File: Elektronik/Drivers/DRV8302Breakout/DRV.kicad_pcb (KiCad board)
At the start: 2 copper layers, 44.4 x 53.3 mm, 55 parts, among them J1 CONN_02X18, J2 CONN_02X12, J3 CONN_02X16, J4 CONN_01X04_MALE, J5 CONN_01X04_MALE, J6 Conn_01x02_Male, U2 TC2117, U3 DRV8302

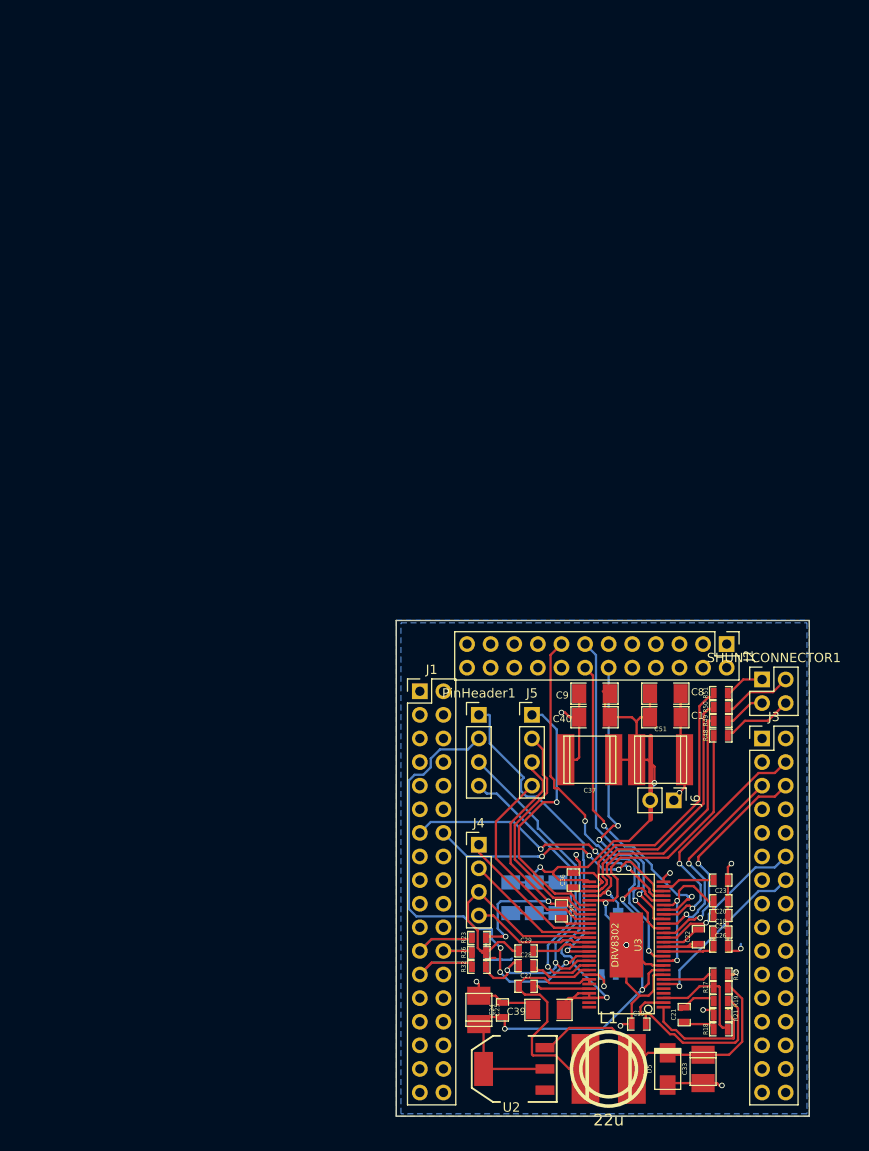
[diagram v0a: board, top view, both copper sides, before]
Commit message: first driver pcb most things routed missnig power connector
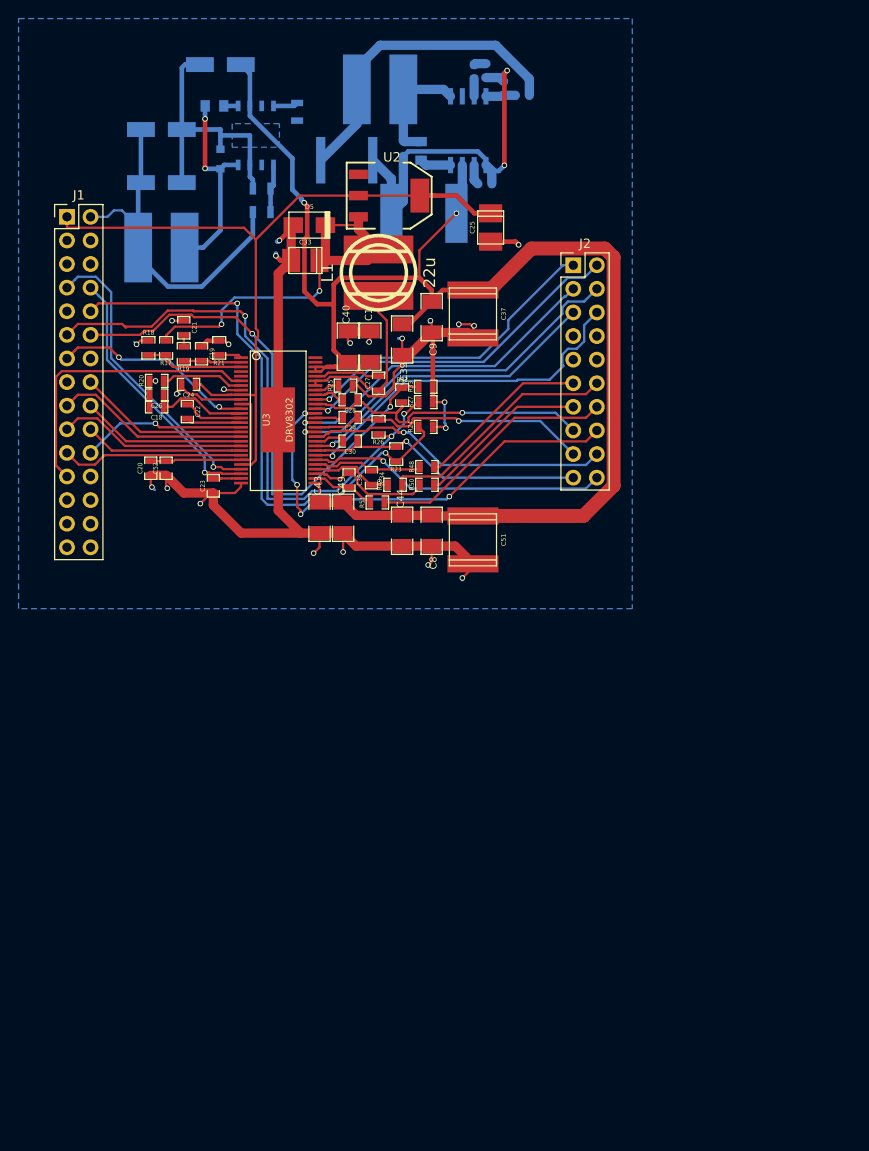
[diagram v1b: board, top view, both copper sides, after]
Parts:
- removed J3: CONN_02X16, Pin_Headers:Pin_Header_Straight_2x16_Pitch2.54mm
- removed J4, J5, PinHeader1: CONN_01X04_MALE, Pin_Headers:Pin_Header_Straight_1x04_Pitch2.54mm
- removed J6: Conn_01x02_Male, Pin_Headers:Pin_Header_Straight_1x02_Pitch2.54mm
- removed SHUNTCONNECTOR1: CONN_01X04_MALE, Pin_Headers:Pin_Header_Straight_2x02_Pitch2.54mm
- added C2: 22μ, Capacitors_SMD:C_2220, B.Cu at (167.4, 38.1)
- added C3: 470pF, Capacitors_SMD:C_0603, B.Cu at (181.1, 28.6)
- added C4: 100nF, Capacitors_SMD:C_0805, B.Cu at (175.4, 37.1)
- added C5: 10μF, Capacitors_SMD:C_2225_HandSoldering, B.Cu at (175.7, 43.8)
- added C6: 10μF, Capacitors_SMD:CP_Elec_5x5.3, B.Cu at (153.8, 27.8)
- added C7: 0.1μF, Capacitors_SMD:C_0805, B.Cu at (153.2, 32.3)
- added Cout1: 33μF, Capacitors_SMD:CP_Elec_5x5.3, B.Cu at (147.4, 34.8)
- added Cout2: 33μF, Capacitors_SMD:CP_Elec_5x5.3, B.Cu at (147.4, 40.5)
- added D1: D_Schottky, Diodes_SMD:D_0603, B.Cu at (173.5, 36.8)
- added D2: D_Schottky_75V, Diodes_SMD:D_0805, B.Cu at (153.8, 38.0)
- added L2: 10μ, w_smd_inductors:inductor_smd_8x5mm, B.Cu at (171.0, 30.5)
- added L3: 10μH, w_smd_inductors:inductor_smd_8x5mm, B.Cu at (147.4, 47.5)
- added R1: 127k, Resistors_SMD:R_0603, B.Cu at (186.3, 31.1)
- added R2: 16k, Resistors_SMD:R_0603, B.Cu at (182.4, 28.5)
- added R3: 40.2k, Resistors_SMD:R_0603, B.Cu at (184.3, 30.4)
- added R4: 200k, Resistors_SMD:R_0603, B.Cu at (182.3, 40.6)
- added RFBB1: 17.8k, Resistors_SMD:R_0805, B.Cu at (158.2, 41.1)
- added RFBT1: 100k, Resistors_SMD:R_0805, B.Cu at (158.2, 43.7)
- added RT1: 41,2k, Resistors_SMD:R_0805, B.Cu at (162.1, 32.9)
- added U1: LMR16020, SMD_Packages:SOIC-8-N, B.Cu at (157.6, 35.4)
- added Ureg1: MP4559, Housings_SOIC:SO-8_5.3x6.2mm_Pitch1.27mm, B.Cu at (180.5, 34.9)
- C34, C43, C44, C49, R24, R25, R27, R33: moved to F.Cu
- J1: value CONN_02X18 -> CONN_CPU; footprint Pin_Headers:Pin_Header_Straight_2x18_Pitch2.54mm -> Pin_Headers:Pin_Header_Straight_2x15_Pitch2.54mm
- J2: value CONN_02X12 -> Conn_POWER; footprint Pin_Headers:Pin_Header_Straight_2x12_Pitch2.54mm -> Pin_Headers:Pin_Header_Straight_2x10_Pitch2.54mm
- moved D5 98.7 mm to (163.4, 45.1), turned to 0 degrees
- moved C33 97.0 mm to (162.9, 48.9), turned to 0 degrees
- moved R18 95.8 mm to (146.1, 58.3), turned to 90 degrees
- moved U2 94.9 mm to (172.0, 41.9), turned to 270 degrees
- moved C21 91.4 mm to (149.9, 56.1), turned to 270 degrees
- moved R17 91.1 mm to (148.0, 58.3), turned to 270 degrees
- moved R19 90.5 mm to (149.9, 58.9), turned to 270 degrees
- moved R21 89.8 mm to (153.7, 58.3), turned to 270 degrees
- moved L1 89.2 mm to (170.8, 50.2), turned to 90 degrees
- moved R20 88.1 mm to (146.9, 61.8), turned to 180 degrees
- moved C19 86.1 mm to (151.8, 58.9), turned to 270 degrees
- moved C26 84.9 mm to (146.9, 63.4), turned to 180 degrees
- moved C25 84.2 mm to (182.9, 45.3), turned to 90 degrees
- moved C18 82.9 mm to (146.9, 64.6), turned to 180 degrees
- moved C22 78.9 mm to (150.2, 65.2), turned to 270 degrees
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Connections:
- J1 pad 1: Net-(J1-Pad1) -> VCC
- J1 pad 10: Net-(J1-Pad10) -> /DRV/SENS1
- J1 pad 11: Net-(J1-Pad11) -> /DRV/SENS2
- J1 pad 12: Net-(J1-Pad12) -> /DRV/SENS3
- J1 pad 13: /CJMCU_PINS/BR_S01 -> /DRV/DC_CAL
- J1 pad 14: /CJMCU_PINS/BR_S02 -> (no net)
- J1 pad 15: /CJMCU_PINS/LED_RED -> (no net)
- J1 pad 16: /CJMCU_PINS/LED_GREEN -> /DRV/H1
- J1 pad 17: Net-(J1-Pad17) -> /DRV/L1
- J1 pad 18: /CJMCU_PINS/MISO_ADC_EXT2 -> /DRV/H2
- J1 pad 19: /CJMCU_PINS/SCK_ADC_EXT -> /DRV/L2
- J1 pad 2: Net-(J1-Pad2) -> /5vReg/5V
- J1 pad 20: /CJMCU_PINS/TX_SDA_NSS -> /DRV/H3
- J1 pad 21: /CJMCU_PINS/ADC_TEMP -> /DRV/L3
- J1 pad 22: Net-(J1-Pad22) -> /DRV/EN_GATE
- J1 pad 23: /CJMCU_PINS/SENS1 -> /DRV/FAULT
- J1 pad 24: /CJMCU_PINS/SENS2 -> (no net)
- J1 pad 25: /CJMCU_PINS/SENS3 -> (no net)
- J1 pad 26: /CJMCU_PINS/AN_IN -> (no net)
- J1 pad 27: Net-(J1-Pad27) -> (no net)
- J1 pad 28: /CJMCU_PINS/TEMP_MOTOR -> (no net)
- J1 pad 29: Net-(J1-Pad29) -> (no net)
- J1 pad 3: Net-(J1-Pad3) -> (no net)
- J1 pad 30: Net-(J1-Pad30) -> (no net)
- J1 pad 4: Net-(J1-Pad4) -> GND
- J1 pad 5: Net-(J1-Pad5) -> (no net)
- J1 pad 6: Net-(J1-Pad6) -> (no net)
- J1 pad 7: /CJMCU_PINS/CAN_TX -> /DRV/BR_SO1
- J1 pad 8: /CJMCU_PINS/CAN_RX -> /DRV/BR_SO2
- J1 pad 9: Net-(J1-Pad9) -> (no net)
- J2 pad 1: Net-(J2-Pad1) -> /DRV/M_H1
- J2 pad 10: Net-(J2-Pad10) -> (no net)
- J2 pad 11: Net-(J2-Pad11) -> /DRV/SH1_A
- J2 pad 12: /CJMCU_PINS/L1 -> /DRV/SH1_B
- J2 pad 13: /CJMCU_PINS/L2 -> /DRV/SH2_A
- J2 pad 14: /CJMCU_PINS/L3 -> /DRV/SH2_B
- J2 pad 15: /CJMCU_PINS/DC_CAL -> /DRV/H1_VS
- J2 pad 16: Net-(J2-Pad16) -> /DRV/H1_LOW
- J2 pad 17: Net-(J2-Pad17) -> /DRV/H2_VS
- J2 pad 18: Net-(J2-Pad18) -> /DRV/H2_LOW
- J2 pad 19: Net-(J2-Pad19) -> /DRV/H3_VS
- J2 pad 2: Net-(J2-Pad2) -> /DRV/M_L1
- J2 pad 20: /CJMCU_PINS/RX_SCL_MOSI -> /DRV/H3_LOW
- J2 pad 3: Net-(J2-Pad3) -> /DRV/M_H2
- J2 pad 4: Net-(J2-Pad4) -> /DRV/M_L2
- J2 pad 5: Net-(J2-Pad5) -> /DRV/M_H3
- J2 pad 6: Net-(J2-Pad6) -> /DRV/M_L3
- J2 pad 7: Net-(J2-Pad7) -> (no net)
- J2 pad 8: Net-(J2-Pad8) -> (no net)
- J2 pad 9: Net-(J2-Pad9) -> (no net)
- R23 pad 2: /CJMCU_PINS/SENS1 -> /DRV/SENS1
- R24 pad 2: /CJMCU_PINS/SENS1 -> /DRV/SENS1
- R26 pad 2: /CJMCU_PINS/SENS2 -> /DRV/SENS2
- R27 pad 2: /CJMCU_PINS/SENS2 -> /DRV/SENS2
- R32 pad 2: /CJMCU_PINS/SENS3 -> /DRV/SENS3
- R33 pad 2: /CJMCU_PINS/SENS3 -> /DRV/SENS3
- U2 pad 1: Net-(U2-Pad1) -> (no net)
- U3 pad 12: /CJMCU_PINS/DC_CAL -> /DRV/DC_CAL
- U3 pad 16: /CJMCU_PINS/EN_GATE -> /DRV/EN_GATE
- U3 pad 17: /CJMCU_PINS/H1 -> /DRV/H1
- U3 pad 18: /CJMCU_PINS/L1 -> /DRV/L1
- U3 pad 19: /CJMCU_PINS/H2 -> /DRV/H2
- U3 pad 20: /CJMCU_PINS/L2 -> /DRV/L2
- U3 pad 21: /CJMCU_PINS/H3 -> /DRV/H3
- U3 pad 22: /CJMCU_PINS/L3 -> /DRV/L3
- U3 pad 25: /CJMCU_PINS/BR_S01 -> /DRV/BR_SO1
- U3 pad 26: /CJMCU_PINS/BR_S02 -> /DRV/BR_SO2
- U3 pad 4: Net-(U3-Pad4) -> (no net)
- U3 pad 5: Net-(U3-Pad5) -> (no net)
- U3 pad 55: Net-(U3-Pad55) -> (no net)
- U3 pad 56: Net-(U3-Pad56) -> (no net)
- U3 pad 6: /CJMCU_PINS/FAULT -> /DRV/FAULT
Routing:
- net GND: track 99.9 -> 237.3 mm, vias 12 -> 26
- net V_SUPPLY: track 88.2 -> 162.5 mm, vias 4 -> 2
- net /DRV/SENS2: track 0.00 -> 64.6 mm, vias 0 -> 3
- net /DRV/SENS1: track 0.00 -> 61.3 mm, vias 0 -> 2
- net /DRV/SENS3: track 0.00 -> 58.3 mm, vias 0 -> 2
- net /CJMCU_PINS/DC_CAL: track 41.5 -> 0.00 mm, vias 2 -> 0
- net /5vReg/5V: track 0.00 -> 40.4 mm
- net /CJMCU_PINS/L2: track 34.8 -> 0.00 mm, vias 1 -> 0
- net /CJMCU_PINS/L1: track 34.5 -> 0.00 mm, vias 3 -> 0
- net /CJMCU_PINS/L3: track 34.4 -> 0.00 mm, vias 2 -> 0
- net +12V: track 0.00 -> 34.3 mm
- net VCC: track 52.2 -> 86.1 mm, vias 3 -> 0
- net /DRV/BR_SO1: track 0.00 -> 32.4 mm, vias 0 -> 1
- net /DRV/FAULT: track 0.00 -> 31.8 mm
- net /CJMCU_PINS/BR_S01: track 30.6 -> 0.00 mm, vias 3 -> 0
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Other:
- board outline removed
- rule pad_to_mask_clearance: 0.2 -> 0

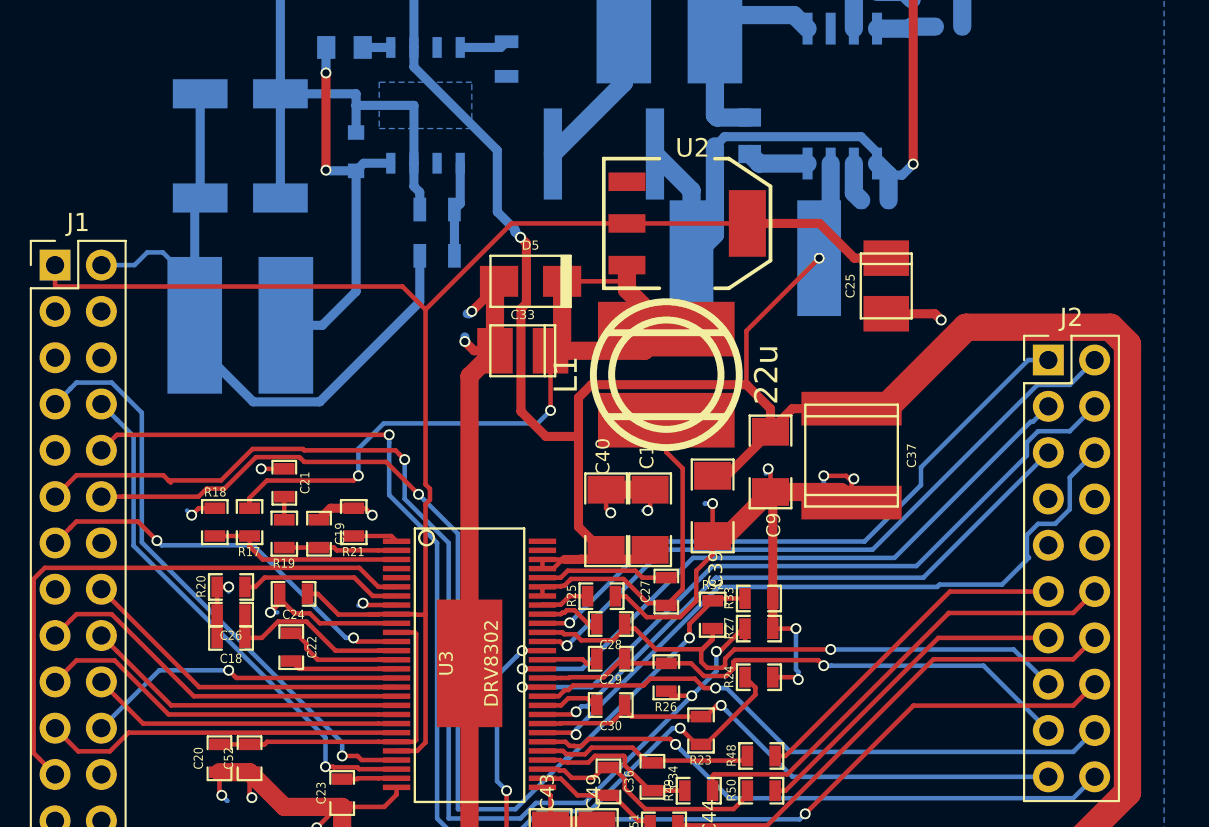
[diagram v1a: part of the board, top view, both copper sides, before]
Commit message: added power connection to driver board
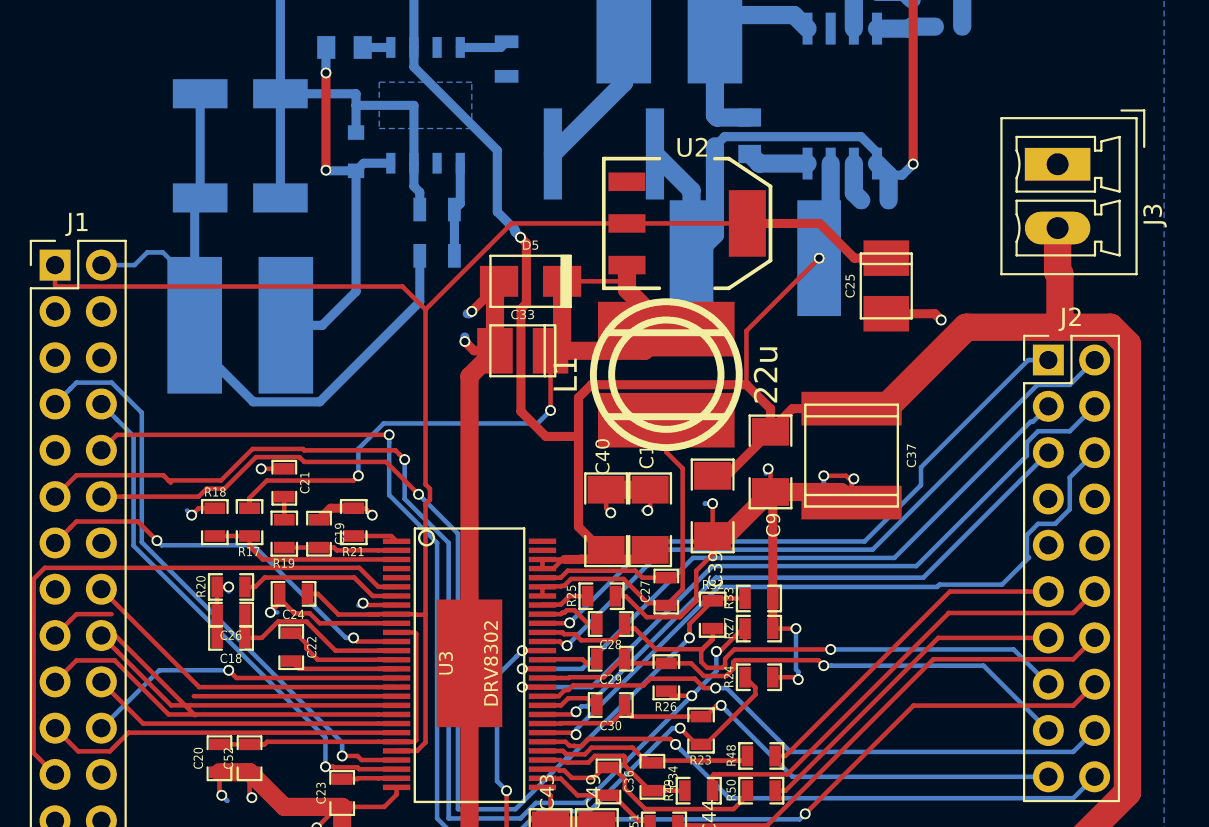
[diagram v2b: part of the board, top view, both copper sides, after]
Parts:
- added J3: Screw_Terminal_1x02, Connectors_Phoenix:PhoenixContact_MCV-G_02x3.50mm_Vertical, F.Cu at (192.3, 38.7)
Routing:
- net /DRV/L1: track 21.1 -> 14.7 mm
- net /DRV/H2: track 17.8 -> 24.1 mm
- net V_SUPPLY: track 162.5 -> 168.0 mm
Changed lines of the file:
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@@
 (kicad_pcb (version 4) (host pcbnew 4.0.6)
   (general
-    (links 164)
-    (no_connects 1)
+    (links 166)
+    (no_connects 3)
     (area 0 0 0 0)
     (thickness 1.6)
     (drawings 2)
-    (tracks 806)
+    (tracks 810)
     (zones 0)
-    (modules 70)
+    (modules 71)
     (nets 67)
   )
   (page A4)
   (layers
-    (0 F.Cu signal)
+    (0 F.Cu signal hide)
     (31 B.Cu signal)
     (32 B.Adhes user)
@@
     (pad_to_mask_clearance 0)
     (aux_axis_origin 0 0)
-    (visible_elements 7FFFFFFF)
+    (visible_elements 7FFFFDF1)
     (pcbplotparams
       (layerselection 0x00030_80000001)
@@
     )
   )
+  (module Connectors_Phoenix:PhoenixContact_MCV-G_02x3.50mm_Vertical (layer F.Cu)
+    (at 192.278 38.664 270)
+    (descr "Generic Phoenix Contact connector footprint for series: MCV-G; number of pins: 02; pin pitch: 3.50mm; Vertical || order number: 1843606 8A 160V")
+    (tags "phoenix_contact connector MCV_01x02_G_3.5mm")
+    (fp_text reference J3 (at 2.75 -5.25 270) (layer F.SilkS)
+      (effects (font (size 1 1) (thickness 0.15)))
+    )
+    (fp_text value Screw_Terminal_1x02 (at 1.75 4 270) (layer F.Fab)
+      (effects (font (size 1 1) (thickness 0.15)))
+    )
+    (fp_arc (start 0 3.95) (end -0.75 2.25) (angle 47.6) (layer F.SilkS) (width 0.12))
+    (fp_arc (start 3.5 3.95) (end 2.75 2.25) (angle 47.6) (layer F.SilkS) (width 0.12))
+    (fp_line (start -2.53 -4.33) (end -2.53 3.08) (layer F.SilkS) (width 0.12))
+    (fp_line (start -2.53 3.08) (end 6.03 3.08) (layer F.SilkS) (width 0.12))
+    (fp_line (start 6.03 3.08) (end 6.03 -4.33) (layer F.SilkS) (width 0.12))
+    (fp_line (start 6.03 -4.33) (end -2.53 -4.33) (layer F.SilkS) (width 0.12))
+    (fp_line (start -2.45 -4.25) (end -2.45 3) (layer F.Fab) (width 0.1))
+    (fp_line (start -2.45 3) (end 5.95 3) (layer F.Fab) (width 0.1))
+    (fp_line (start 5.95 3) (end 5.95 -4.25) (layer F.Fab) (width 0.1))
+    (fp_line (start 5.95 -4.25) (end -2.45 -4.25) (layer F.Fab) (width 0.1))
+    (fp_line (start -0.75 2.25) (end -1.5 2.25) (layer F.SilkS) (width 0.12))
+    (fp_line (start -1.5 2.25) (end -1.5 -2.05) (layer F.SilkS) (width 0.12))
+    (fp_line (start -1.5 -2.05) (end -0.75 -2.05) (layer F.SilkS) (width 0.12))
+    (fp_line (start -0.75 -2.05) (end -0.75 -2.4) (layer F.SilkS) (width 0.12))
+    (fp_line (start -0.75 -2.4) (end -1.25 -2.4) (layer F.SilkS) (width 0.12))
+    (fp_line (start -1.25 -2.4) (end -1.5 -3.4) (layer F.SilkS) (width 0.12))
+    (fp_line (start -1.5 -3.4) (end 1.5 -3.4) (layer F.SilkS) (width 0.12))
+    (fp_line (start 1.5 -3.4) (end 1.25 -2.4) (layer F.SilkS) (width 0.12))
+    (fp_line (start 1.25 -2.4) (end 0.75 -2.4) (layer F.SilkS) (width 0.12))
+    (fp_line (start 0.75 -2.4) (end 0.75 -2.05) (layer F.SilkS) (width 0.12))
+    (fp_line (start 0.75 -2.05) (end 1.5 -2.05) (layer F.SilkS) (width 0.12))
+    (fp_line (start 1.5 -2.05) (end 1.5 2.25) (layer F.SilkS) (width 0.12))
+    (fp_line (start 1.5 2.25) (end 0.75 2.25) (layer F.SilkS) (width 0.12))
+    (fp_line (start 2.75 2.25) (end 2 2.25) (layer F.SilkS) (width 0.12))
+    (fp_line (start 2 2.25) (end 2 -2.05) (layer F.SilkS) (width 0.12))
+    (fp_line (start 2 -2.05) (end 2.75 -2.05) (layer F.SilkS) (width 0.12))
+    (fp_line (start 2.75 -2.05) (end 2.75 -2.4) (layer F.SilkS) (width 0.12))
+    (fp_line (start 2.75 -2.4) (end 2.25 -2.4) (layer F.SilkS) (width 0.12))
+    (fp_line (start 2.25 -2.4) (end 2 -3.4) (layer F.SilkS) (width 0.12))
+    (fp_line (start 2 -3.4) (end 5 -3.4) (layer F.SilkS) (width 0.12))
+    (fp_line (start 5 -3.4) (end 4.75 -2.4) (layer F.SilkS) (width 0.12))
+    (fp_line (start 4.75 -2.4) (end 4.25 -2.4) (layer F.SilkS) (width 0.12))
+    (fp_line (start 4.25 -2.4) (end 4.25 -2.05) (layer F.SilkS) (width 0.12))
+    (fp_line (start 4.25 -2.05) (end 5 -2.05) (layer F.SilkS) (width 0.12))
+    (fp_line (start 5 -2.05) (end 5 2.25) (layer F.SilkS) (width 0.12))
+    (fp_line (start 5 2.25) (end 4.25 2.25) (layer F.SilkS) (width 0.12))
+    (fp_line (start -2.95 -4.75) (end -2.95 3.5) (layer F.CrtYd) (width 0.05))
+    (fp_line (start -2.95 3.5) (end 6.45 3.5) (layer F.CrtYd) (width 0.05))
+    (fp_line (start 6.45 3.5) (end 6.45 -4.75) (layer F.CrtYd) (width 0.05))
+    (fp_line (start 6.45 -4.75) (end -2.95 -4.75) (layer F.CrtYd) (width 0.05))
+    (fp_line (start -2.95 -3.5) (end -2.95 -4.75) (layer F.SilkS) (width 0.12))
+    (fp_line (start -2.95 -4.75) (end -0.95 -4.75) (layer F.SilkS) (width 0.12))
+    (fp_line (start -2.95 -3.5) (end -2.95 -4.75) (layer F.Fab) (width 0.1))
+    (fp_line (start -2.95 -4.75) (end -0.95 -4.75) (layer F.Fab) (width 0.1))
+    (fp_text user %R (at 1.75 -3 270) (layer F.Fab)
+      (effects (font (size 1 1) (thickness 0.15)))
+    )
+    (pad 1 thru_hole rect (at 0 0 270) (size 1.8 3.6) (drill 1.2) (layers *.Cu *.Mask)
+      (net 1 GND))
+    (pad 2 thru_hole oval (at 3.5 0 270) (size 1.8 3.6) (drill 1.2) (layers *.Cu *.Mask)
+      (net 2 V_SUPPLY))
+    (model ${KISYS3DMOD}/Connectors_Phoenix.3dshapes/PhoenixContact_MCV-G_02x3.50mm_Vertical.wrl
+      (at (xyz 0 0 0))
+      (scale (xyz 1 1 1))
+      (rotate (xyz 0 0 0))
+    )
+  )
   (dimension 66.167122 (width 0.3) (layer Dwgs.User)
     (gr_text "66.167 mm" (at 165.157258 19.544191 0.1099725704) (layer Dwgs.User)
@@
   (segment (start 149.987 27.813) (end 149.647 28.153) (width 0.5) (layer B.Cu) (net 1))
   (segment (start 149.647 34.798) (end 149.647 40.513) (width 0.5) (layer B.Cu) (net 1))
+  (segment (start 187.266991 47.602999) (end 192.405 47.602999) (width 1.5) (layer F.Cu) (net 2))
+  (segment (start 192.405 47.602999) (end 195.174001 47.602999) (width 1.5) (layer F.Cu) (net 2))
+  (segment (start 192.278 42.164) (end 192.278 44.564) (width 1.5) (layer F.Cu) (net 2))
+  (segment (start 192.278 44.564) (end 192.405 44.691) (width 1.5) (layer F.Cu) (net 2))
+  (segment (start 192.405 44.691) (end 192.405 47.602999) (width 1.5) (layer F.Cu) (net 2))
   (segment (start 180.975 52.07) (end 182.79999 52.07) (width 1.5) (layer F.Cu) (net 2))
   (segment (start 182.79999 52.07) (end 187.266991 47.602999) (width 1.5) (layer F.Cu) (net 2))
-  (segment (start 187.266991 47.602999) (end 195.174001 47.602999) (width 1.5) (layer F.Cu) (net 2))
   (segment (start 195.174001 47.602999) (end 196.110001 48.538999) (width 1.5) (layer F.Cu) (net 2))
   (segment (start 196.110001 48.538999) (end 196.110001 73.127001) (width 1.5) (layer F.Cu) (net 2))
@@
   (segment (start 138.462001 63.340999) (end 138.136999 63.666001) (width 0.25) (layer F.Cu) (net 39))
   (segment (start 140.391001 63.340999) (end 138.462001 63.340999) (width 0.25) (layer F.Cu) (net 39))
-  (segment (start 144.893402 67.8434) (end 140.391001 63.340999) (width 0.25) (layer F.Cu) (net 39))
   (segment (start 138.136999 63.666001) (end 137.287 64.516) (width 0.25) (layer F.Cu) (net 39))
+  (segment (start 144.964401 68.891401) (end 140.462 64.389) (width 0.25) (layer F.Cu) (net 40))
   (segment (start 140.676999 65.365999) (end 139.827 64.516) (width 0.25) (layer F.Cu) (net 40))
   (segment (start 143.65478 68.34378) (end 140.676999 65.365999) (width 0.25) (layer F.Cu) (net 40))
